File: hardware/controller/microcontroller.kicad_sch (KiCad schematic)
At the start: 39 parts, among them J1 USB_C_Receptacle_USB2.0_14P, J2 IDC-10, SW1 SW_Push, SW2 SW_Push, SW3 SW_Push, U1 USBLC6-2SC6, U2 ESP32-C3-WROOM-02, U3 STM32U535RET6, U4 nRF24L01+ 2.4Gz Mini SMD, Y1 8MHz

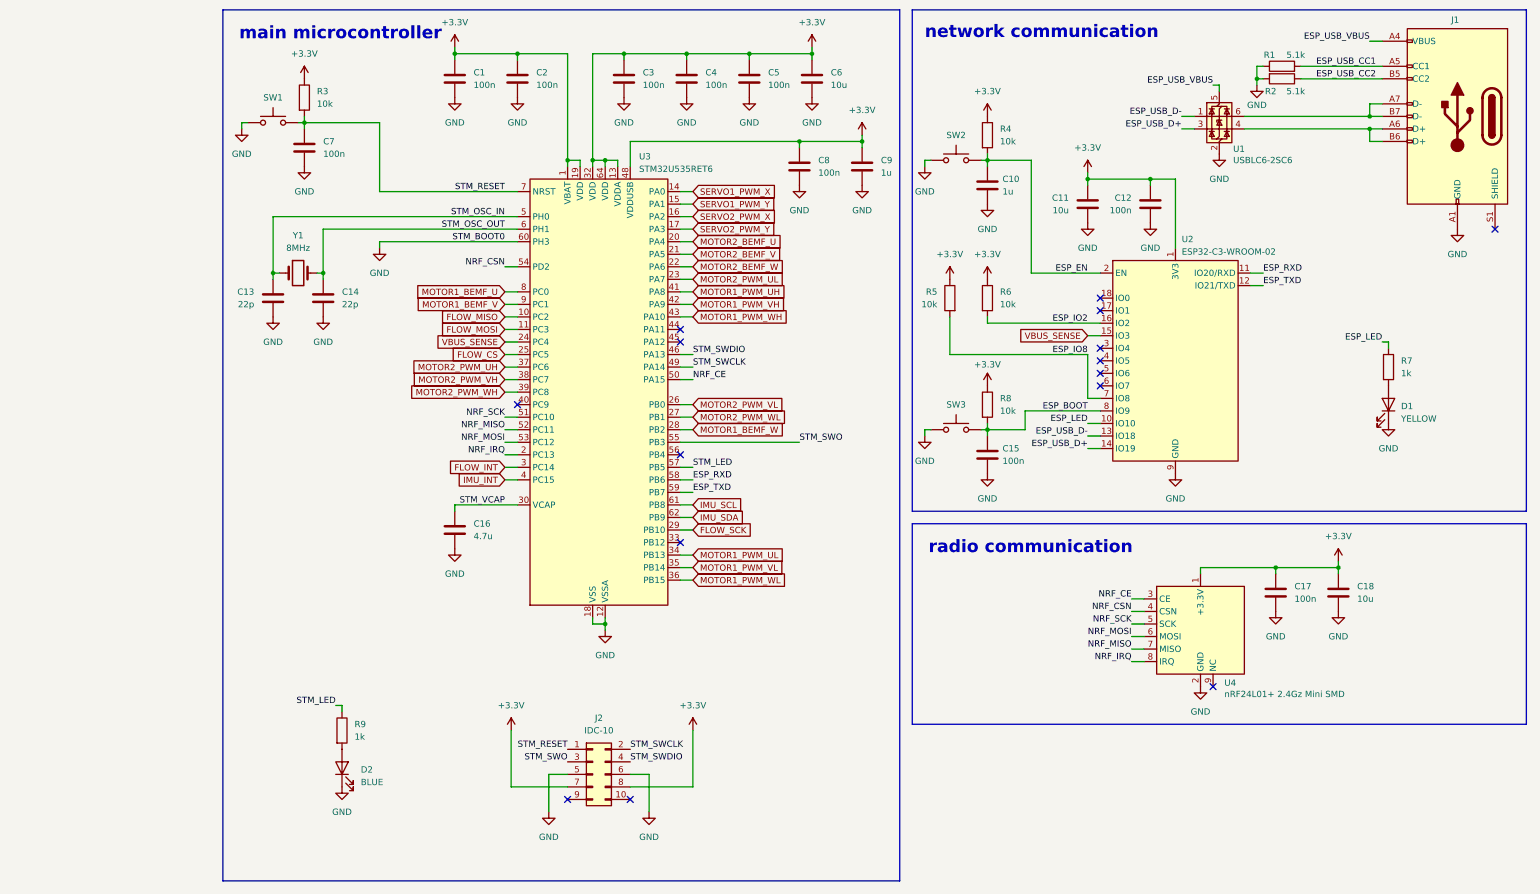
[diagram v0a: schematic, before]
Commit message: full layout, edge power switch
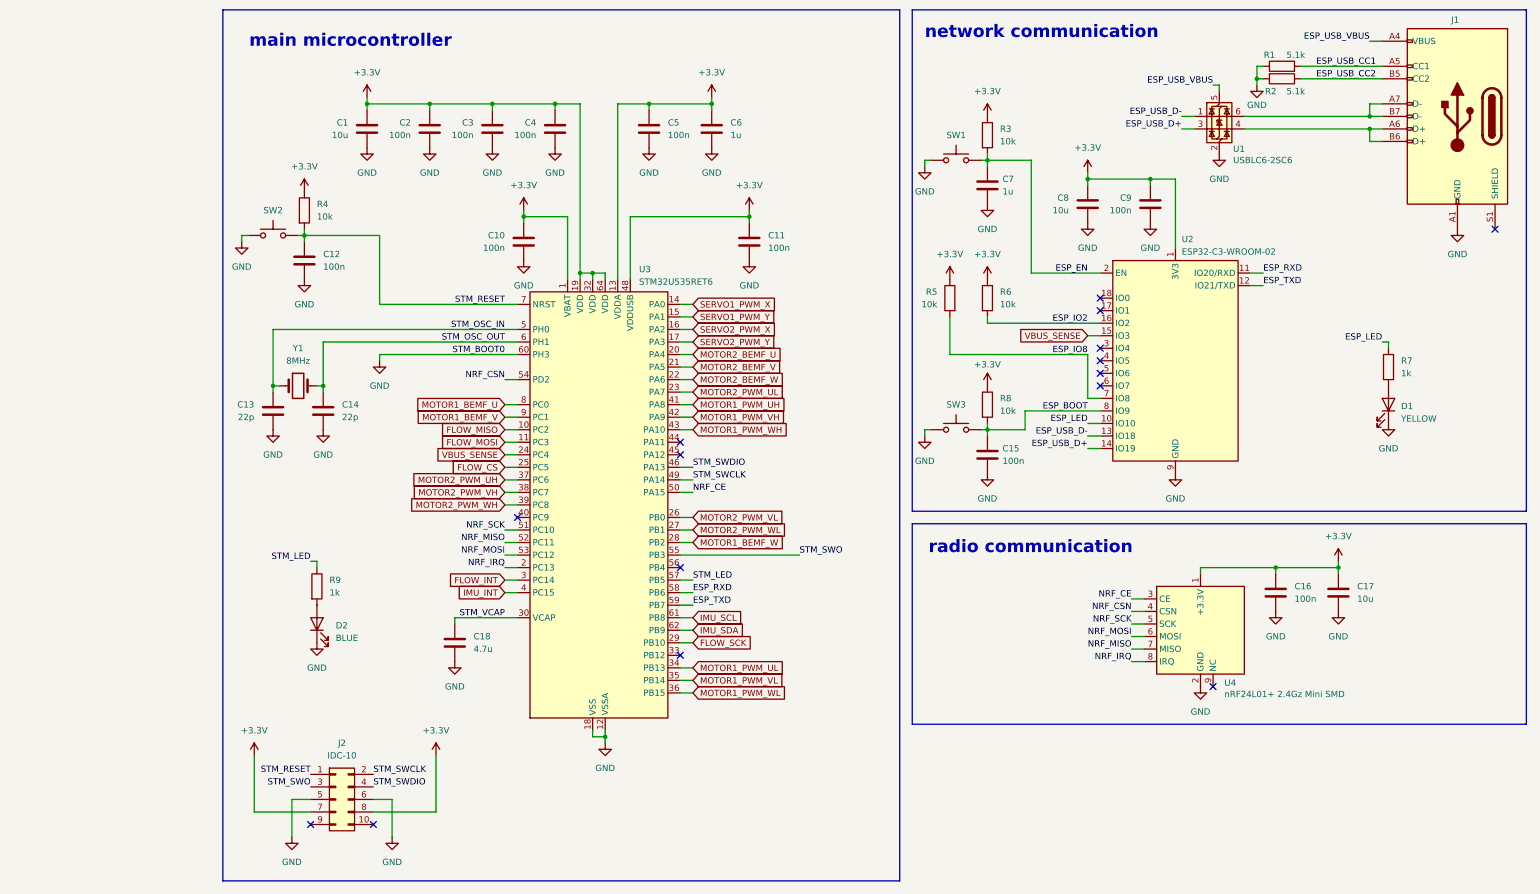
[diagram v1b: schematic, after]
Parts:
- removed C2: 100n, Capacitor_SMD:C_0603_1608Metric, symbol Device:C
- added C11: 100n, Capacitor_SMD:C_0603_1608Metric, symbol Device:C
- renumbered C6 to C1, C1 to C10, C7 to C12, C17 to C16, C18 to C17, C16 to C18, C5 to C2, C4 to C3, C3 to C4, C8 to C5, C9 to C6, C10 to C7, C11 to C8, C12 to C9, R4 to R3, R3 to R4, SW2 to SW1, SW1 to SW2
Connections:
- net +3.3V: now also C11.1
- net GND: now also C11.2
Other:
- moved on the sheet: C1, C10, C12, C13, C14, C18, C2, C3, C4, C5, C6, D2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

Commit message: wip
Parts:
- removed C15, C16: 100n, Capacitor_SMD:C_0603_1608Metric, symbol Device:C
- removed C17, C8: 10u, Capacitor_SMD:C_0603_1608Metric, symbol Device:C
- removed C7: 1u, Capacitor_SMD:C_0603_1608Metric, symbol Device:C
- removed SW3: SW_Push, hogger2:spst_6x3mm, symbol Switch:SW_Push
- removed U3: STM32U535RET6, Package_QFP:LQFP-64_10x10mm_P0.5mm, symbol MCU_ST_STM32U5:STM32U535RETx
- removed U4: nRF24L01+ 2.4Gz Mini SMD, hogger2:nRF24L01p_Mini_SMD, symbol hogger2:nRF24L01+_2.4GHz_Mini_SMD
- added C15, C16, C17, C7, C8: 100uF, symbol Device:C_Polarized
- added C80: 100n, Capacitor_SMD:C_0603_1608Metric, symbol Device:C
- added C81: 2.2u, Capacitor_SMD:C_0603_1608Metric, symbol Device:C
- added R52: 10k, Resistor_SMD:R_0603_1608Metric, symbol Device:R
- added U4: STM32H523RETx, Package_QFP:LQFP-64_10x10mm_P0.5mm, symbol MCU_ST_STM32H5:STM32H523RETx
- C1: value 10u -> 4.7u
- C18: value 4.7u -> 2.2u
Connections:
- net +3.3V: now also C15.1, C16.1, C17.1, C7.1, C8.1, R52.1, U4.1 (VBAT), U4.13 (VDDA), U4.19 (VDD), U4.32 (VDD), U4.48 (VDD), U4.64 (VDD)
- net ESP_EN: no longer R3.2, SW1.2, U2.2 (EN)
- net FLOW_CS: now also U4.50 (PA15(JTDI))
- net FLOW_INT: now also U4.2 (PC13)
- net FLOW_MISO: now also U4.52 (PC11)
- net FLOW_MOSI: now also U4.53 (PC12)
- net FLOW_SCK: now also U4.51 (PC10)
- net GND: now also C15.2, C16.2, C17.2, C7.2, C8.2, C80.2, C81.2, U4.12 (VSSA), U4.18 (VSS), U4.31 (VSS), U4.47 (VSS), U4.60 (BOOT0), U4.63 (VSS)
- net IMU_INT: now also U4.3 (PC14)
- net MOTOR1_BEMF_U: now also U4.14 (PA0)
- net MOTOR1_BEMF_V: now also U4.15 (PA1)
- net MOTOR1_BEMF_W: now also U4.16 (PA2)
- net MOTOR1_PWM_UH: now also U4.41 (PA8)
- net MOTOR1_PWM_UL: now also U4.34 (PB13)
- net MOTOR1_PWM_VH: now also U4.42 (PA9)
- net MOTOR1_PWM_VL: now also U4.35 (PB14)
- net MOTOR1_PWM_WH: now also U4.43 (PA10)
- net MOTOR1_PWM_WL: now also U4.36 (PB15)
- net MOTOR2_BEMF_U: now also U4.20 (PA4)
- net MOTOR2_BEMF_V: now also U4.21 (PA5)
- net MOTOR2_BEMF_W: now also U4.22 (PA6)
- net MOTOR2_PWM_UH: now also U4.37 (PC6)
- net MOTOR2_PWM_UL: now also U4.23 (PA7)
- net MOTOR2_PWM_VH: now also U4.38 (PC7)
- net MOTOR2_PWM_VL: now also U4.26 (PB0)
- net MOTOR2_PWM_WH: now also U4.39 (PC8)
- net MOTOR2_PWM_WL: now also U4.27 (PB1)
- net STM_OSC_IN: now also U4.5 (PH0)
- net STM_OSC_OUT: now also U4.6 (PH1)
- net STM_RESET: now also U4.7 (NRST)
- net STM_SWCLK: now also U4.49 (PA14(JTCK)
- net STM_SWDIO: now also U4.46 (PA13(JTMS)
- net STM_SWO: now also U4.55 (PB3(JTDO)
- net STM_VCAP: now also C81.1, U4.30 (VCAP), U4.62 (VCAP)
- net VBUS_SENSE: now also U4.11 (PC3); no longer U2.15 (IO3)
- net ESP_RXD: no longer names the net of U2.11 (IO20/RXD)
- net ESP_TXD: no longer names the net of U2.12 (IO21/TXD)
- net ESP_USB_VBUS renamed +5V
- new net ESP_CS: U4.17 (PA3)
- new net ESP_MISO: U4.10 (PC2)
- new net ESP_MOSI: U4.9 (PC1)
- new net ESP_RDY: U4.8 (PC0)
- new net ESP_RESET: R3.2, U2.2 (EN)
- new net ESP_SCK: U4.29 (PB10)
- new net MAG_INT: U4.4 (PC15)
- new net SERVO1_DATA: U4.58 (PB6)
- new net SERVO2_DATA: U4.57 (PB5)
- new net STM_BUTTON: C80.1, R52.2, SW1.2
- no-connect marks 15 -> 12
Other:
- note added: "host microcontroller"
- note added: "network microcontroller"
- note removed: "main microcontroller"
- note removed: "network communication"
- note removed: "radio communication"
- moved on the sheet: C1, C10, C12, C18, C2, C3, C4, C5, C6, C9, D1, D2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

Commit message: wip
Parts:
- removed C80: 100n, Capacitor_SMD:C_0603_1608Metric, symbol Device:C
- removed R52: 10k, Resistor_SMD:R_0603_1608Metric, symbol Device:R
- removed SW1: SW_Push, hogger2:spst_6x3mm, symbol Switch:SW_Push
- C15, C16, C17, C7, C8: value 100uF -> 100u
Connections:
- net ESP_RESET is gone; now on net ESP_EN: R3.2, U2.2 (EN)
- net ESP_CS: now also U2.6 (IO7), U4.20 (PA4); no longer U4.17 (PA3)
- net ESP_EN: now also U4.45 (PA12)
- net ESP_HANDSHAKE: now also U2.15 (IO3), U4.44 (PA11)
- net ESP_LED: now also U2.18 (IO0); no longer U2.10 (IO10)
- net ESP_MISO: now also U2.4 (IO5), U4.56 (PB4(NJTRST)); no longer U4.10 (PC2)
- net ESP_MOSI: now also U2.3 (IO4), U4.57 (PB5); no longer U4.9 (PC1)
- net ESP_RDY: now also U2.10 (IO10), U4.28 (PB2); no longer U4.8 (PC0)
- net ESP_SCK: now also U2.5 (IO6), U4.55 (PB3(JTDO); no longer U4.29 (PB10)
- net FLOW_CS: now also U4.61 (PB8); no longer U4.50 (PA15(JTDI))
- net IMU_SCL: now also U4.58 (PB6)
- net IMU_SDA: now also U4.59 (PB7)
- net MAG_SCL: now also U4.29 (PB10)
- net MAG_SDA: now also U4.33 (PB12)
- net MOTOR1_BEMF_U: now also U4.8 (PC0); no longer U4.14 (PA0)
- net MOTOR1_BEMF_V: now also U4.9 (PC1); no longer U4.15 (PA1)
- net MOTOR1_BEMF_W: now also U4.10 (PC2); no longer U4.16 (PA2)
- net MOTOR2_BEMF_U: now also U4.21 (PA5); no longer U4.20 (PA4)
- net MOTOR2_BEMF_V: now also U4.22 (PA6); no longer U4.21 (PA5)
- net MOTOR2_BEMF_W: now also U4.24 (PC4); no longer U4.22 (PA6)
- net SERVO1_DATA: now also U4.50 (PA15(JTDI)); no longer U4.58 (PB6)
- net SERVO2_DATA: now also U4.14 (PA0); no longer U4.57 (PB5)
- net STM_LED: now also U4.15 (PA1)
- net ESP_RXD: now reaches U2.11 (IO20/RXD)
- net ESP_RXD: now also U4.16 (PA2)
- net ESP_TXD: now reaches U2.12 (IO21/TXD)
- net ESP_TXD: now also U4.17 (PA3)
- net STM_SWO: no longer names the net of J2.3 (Pin_3)
- net STM_SWO: no longer U4.55 (PB3(JTDO)
- no-connect marks 12 -> 8
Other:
- moved on the sheet: C12, C15, C16, C17, C7, C8, C9, D1, R3, R4, R5, R6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
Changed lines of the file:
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@@
 	(title_block
 		(title "Hogger2 Controller")
-		(date "2025-02-18")
+		(date "2025-02-19")
 		(rev "V1.1")
 		(comment 4 "Author: Eryk Możdżeń")

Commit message: wip
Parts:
- removed C15, C16, C17, C7, C8: 100u, symbol Device:C_Polarized
- added C10, C11, C12, C13, C14: 100u, Capacitor_SMD:C_1206_3216Metric, symbol Device:C
- renumbered C9 to C15, C13 to C16, C14 to C17, C81 to C18, C18 to C19, C11 to C2, C2 to C3, C3 to C4, C4 to C5, C10 to C6, C5 to C7, C6 to C8, C12 to C9, R7 to R3, R8 to R5, R5 to R6, R6 to R7, R3 to R8, SW2 to SW1, U4 to U2, U2 to U3
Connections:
- net +3.3V: now also C10.1, C11.1, C12.1, C13.1, C14.1
- net GND: now also C10.2, C11.2, C12.2, C13.2, C14.2
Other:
- moved on the sheet: C15, D2, J2, R5, R6, R7, R8, R9, U3
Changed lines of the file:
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@@
 	(title_block
 		(title "Hogger2 Controller")
-		(date "2025-02-19")
+		(date "2025-02-20")
 		(rev "V1.1")
 		(comment 4 "Author: Eryk Możdżeń")

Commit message: wip better pinout
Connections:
- net FLOW_INT: now also U2.54 (PD2); no longer U2.2 (PC13)
- net IMU_INT: now also U2.40 (PC9); no longer U2.3 (PC14)
- net IMU_SCL: now also U2.29 (PB10); no longer U2.58 (PB6)
- net IMU_SDA: now also U2.33 (PB12); no longer U2.59 (PB7)
- net MAG_SCL: now also U2.58 (PB6); no longer U2.29 (PB10)
- net MAG_SDA: now also U2.59 (PB7); no longer U2.33 (PB12)
- net MOTOR1_BEMF_U: now also U2.21 (PA5); no longer U2.8 (PC0)
- net MOTOR1_BEMF_V: now also U2.22 (PA6); no longer U2.9 (PC1)
- net MOTOR1_BEMF_W: now also U2.24 (PC4); no longer U2.10 (PC2)
- net MOTOR1_PWM_UH: now also U2.37 (PC6); no longer U2.41 (PA8)
- net MOTOR1_PWM_UL: now also U2.23 (PA7); no longer U2.34 (PB13)
- net MOTOR1_PWM_VH: now also U2.38 (PC7); no longer U2.42 (PA9)
- net MOTOR1_PWM_VL: now also U2.26 (PB0); no longer U2.35 (PB14)
- net MOTOR1_PWM_WH: now also U2.39 (PC8); no longer U2.43 (PA10)
- net MOTOR1_PWM_WL: now also U2.27 (PB1); no longer U2.36 (PB15)
- net MOTOR2_BEMF_U: now also U2.8 (PC0); no longer U2.21 (PA5)
- net MOTOR2_BEMF_V: now also U2.9 (PC1); no longer U2.22 (PA6)
- net MOTOR2_BEMF_W: now also U2.10 (PC2); no longer U2.24 (PC4)
- net MOTOR2_PWM_UH: now also U2.41 (PA8); no longer U2.37 (PC6)
- net MOTOR2_PWM_UL: now also U2.34 (PB13); no longer U2.23 (PA7)
- net MOTOR2_PWM_VH: now also U2.42 (PA9); no longer U2.38 (PC7)
- net MOTOR2_PWM_VL: now also U2.35 (PB14); no longer U2.26 (PB0)
- net MOTOR2_PWM_WH: now also U2.43 (PA10); no longer U2.39 (PC8)
- net MOTOR2_PWM_WL: now also U2.36 (PB15); no longer U2.27 (PB1)
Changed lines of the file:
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@@
 	(title_block
 		(title "Hogger2 Controller")
-		(date "2025-03-08")
+		(date "2025-03-09")
 		(rev "V1.1")
 		(comment 4 "Author: Eryk Możdżeń")
